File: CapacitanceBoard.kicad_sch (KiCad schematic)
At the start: 1 part, among them U1 AD7150BRMZ

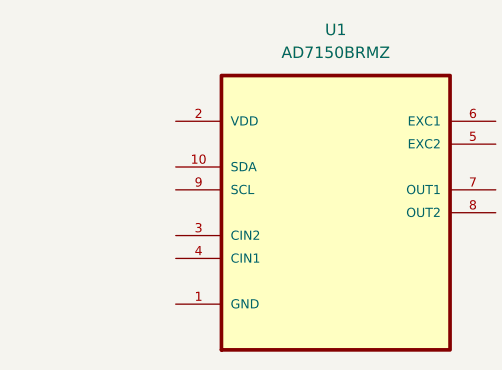
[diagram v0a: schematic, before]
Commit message: Added Mounting Holes
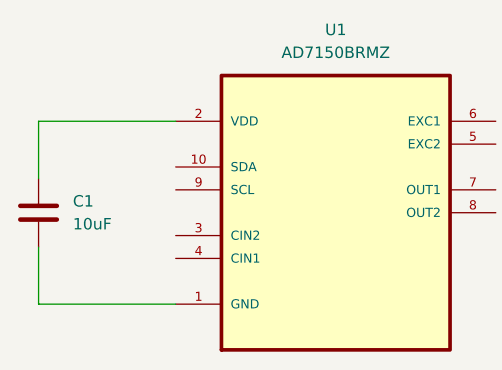
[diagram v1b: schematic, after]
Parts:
- added C1: 10uF, symbol Device:C
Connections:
- net at U1.1 (GND): now also C1.2
- net at U1.2 (VDD): now also C1.1
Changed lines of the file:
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@@
 (kicad_sch (version 20230121) (generator eeschema)
   (paper "A4")
+  (wire (pts (xy 151.13 110.49) (xy 151.13 104.14))
+    (stroke (width 0) (type default))
+  )
+  (wire (pts (xy 151.13 118.11) (xy 151.13 124.46))
+    (stroke (width 0) (type default))
+  )
+  (wire (pts (xy 151.13 104.14) (xy 166.37 104.14))
+    (stroke (width 0) (type default))
+  )
+  (wire (pts (xy 151.13 124.46) (xy 166.37 124.46))
+    (stroke (width 0) (type default))
+  )
+  (symbol (lib_id "Device:C") (at 151.13 114.3 0) (unit 1)
+    (in_bom yes) (on_board yes) (dnp no) (fields_autoplaced)
+    (property "Reference" "C1" (at 154.94 113.03 0)
+      (effects (font (size 1.27 1.27)) (justify left))
+    )
+    (property "Value" "10uF" (at 154.94 115.57 0)
+      (effects (font (size 1.27 1.27)) (justify left))
+    )
+    (property "Footprint" "" (at 152.0952 118.11 0)
+      (effects (font (size 1.27 1.27)) hide)
+    )
+    (property "Datasheet" "~" (at 151.13 114.3 0)
+      (effects (font (size 1.27 1.27)) hide)
+    )
+    (pin "2")
+    (pin "1")
+    (instances
+      (project "CapacitanceBoard"
+        (path "/0af505e0-95df-41c2-86c6-c66100d85f83"
+          (reference "C1") (unit 1)
+        )
+      )
+    )
+  )
   (symbol (lib_id "AD7150BRMZ:AD7150BRMZ") (at 184.15 111.76 0) (unit 1)
     (in_bom yes) (on_board yes) (dnp no) (fields_autoplaced)

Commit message: Added Schematic Files
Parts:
- added C: 47p, symbol Device:C
- added C: 68p, symbol Device:C
- added C2: 10u, symbol Device:C
- added C4: 22p, symbol Device:C
- added R: 39k, symbol Device:R
- added R1, R2: 1k, symbol Device:R
- added R3: 10k, symbol Device:R
- added R4: 82k, symbol Device:R
- C1: value 10uF -> 0.1u
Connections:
- net Earth: now reaches C1.1
- net Earth: now also U1.1 (GND), C.1, C.1, C2.1, C4.1; no longer U1.2 (VDD)
- net VDD: now reaches C1.2
- net VDD: now also U1.2 (VDD), C2.2, R1.2, R2.2; no longer U1.1 (GND)
- net SDA: now reaches U1.10 (SDA)
- net SDA: now also R1.1
- net at U1.4 (CIN1): now also C4.2, R4.1
- net at U1.6 (EXC1): now also C.2, R3.2
- net SCL: now reaches U1.9 (SCL)
- net SCL: now also R2.1
- new net: C.2, R.1, R4.2
- new net Probe: R.2, R3.1

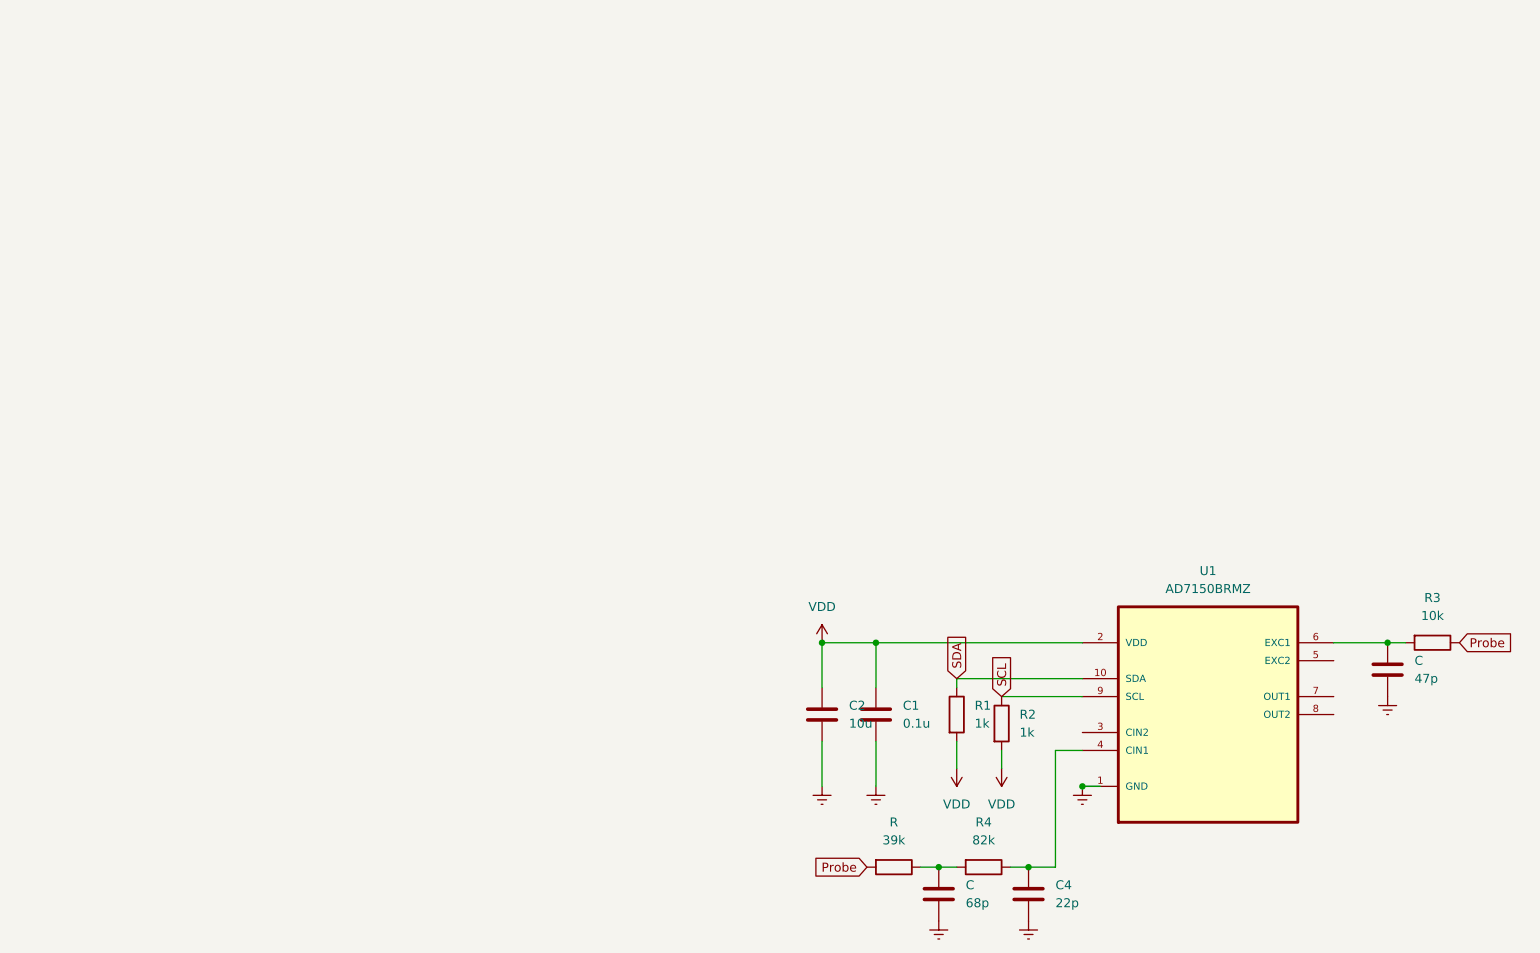
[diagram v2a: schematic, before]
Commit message: Improved schematic and updated PCB references and layout.
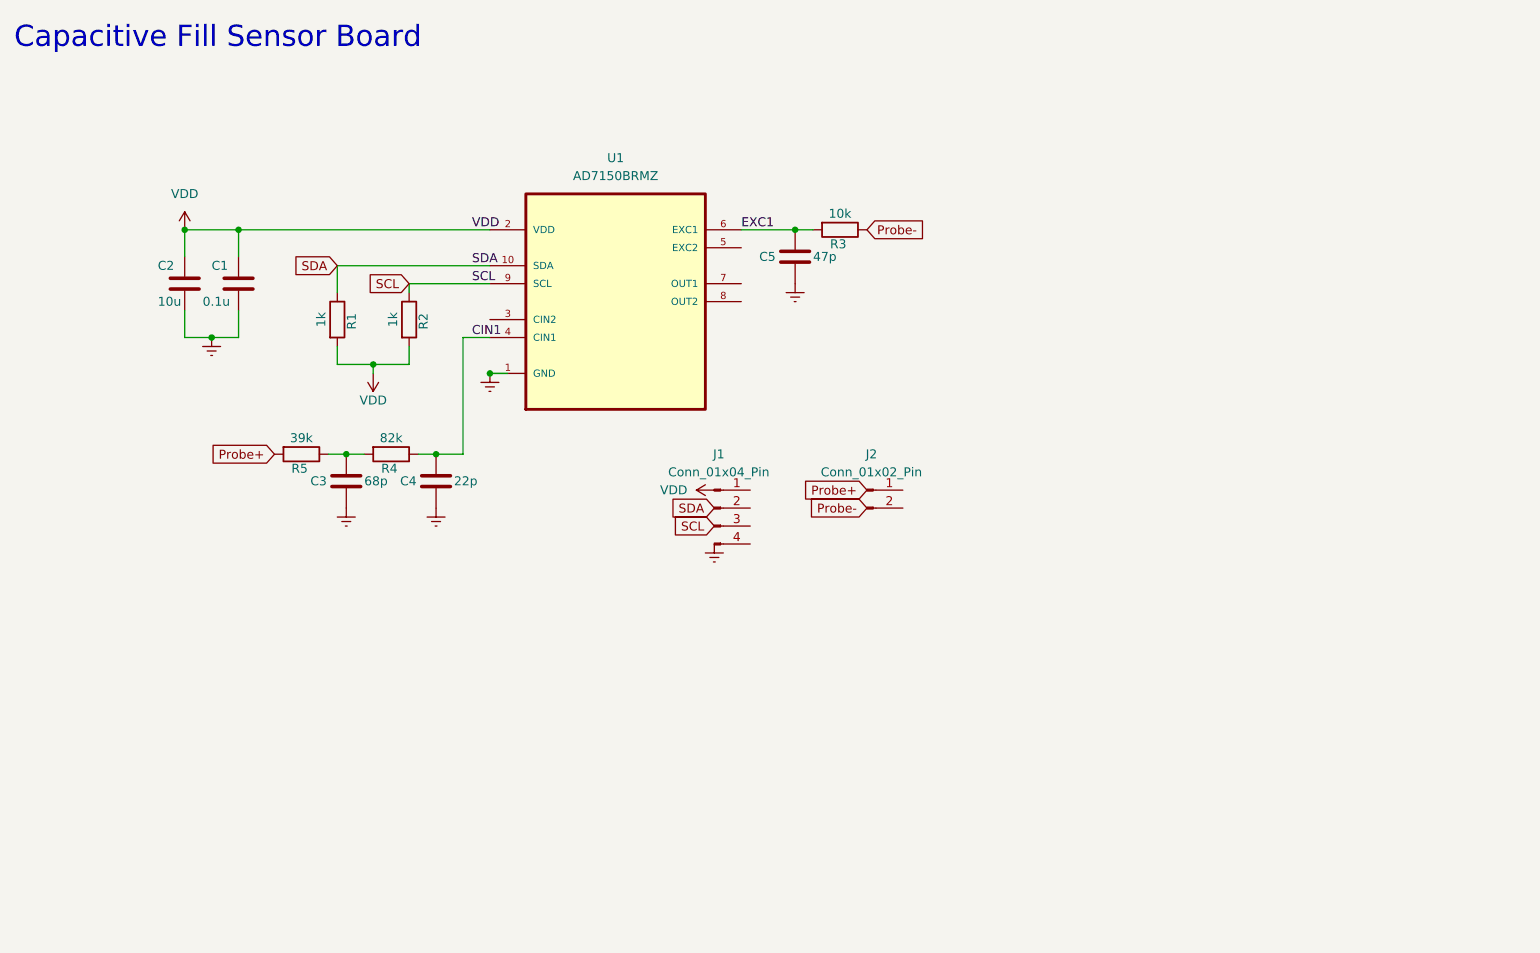
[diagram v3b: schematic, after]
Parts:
- removed C: 47p, symbol Device:C
- removed C: 68p, symbol Device:C
- removed R: 39k, symbol Device:R
- added C3: 68p, Capacitor_SMD:C_0402_1005Metric, symbol Device:C
- added C5: 47p, Capacitor_SMD:C_0402_1005Metric, symbol Device:C
- added J1: Conn_01x04_Pin, Connector_JST:JST_XH_S4B-XH-A_1x04_P2.50mm_Horizontal, symbol Connector:Conn_01x04_Pin
- added J2: Conn_01x02_Pin, Connector_JST:JST_XH_S2B-XH-A_1x02_P2.50mm_Horizontal, symbol Connector:Conn_01x02_Pin
- added R5: 39k, Resistor_SMD:R_0402_1005Metric, symbol Device:R
- C1, C2, C4: footprint (none) -> Capacitor_SMD:C_0402_1005Metric
- R1, R2, R3, R4: footprint (none) -> Resistor_SMD:R_0402_1005Metric
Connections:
- net Earth: now also C1.2, C2.2, C4.2, C3.2, C5.2; no longer C1.1, C2.1, C4.1
- net VDD: now also C1.1, C2.1; no longer C1.2, C2.2
- net EXC1: now reaches R3.2, U1.6 (EXC1)
- net EXC1: now also C5.1
- net CIN1: now reaches R4.1, U1.4 (CIN1)
- net CIN1: now also C4.1; no longer C4.2
- net at R4.2: now also C3.1, R5.1
- net Probe renamed Probe-
- new net Probe+: R5.2
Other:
- note added: "Capacitive Fill Sensor Board"

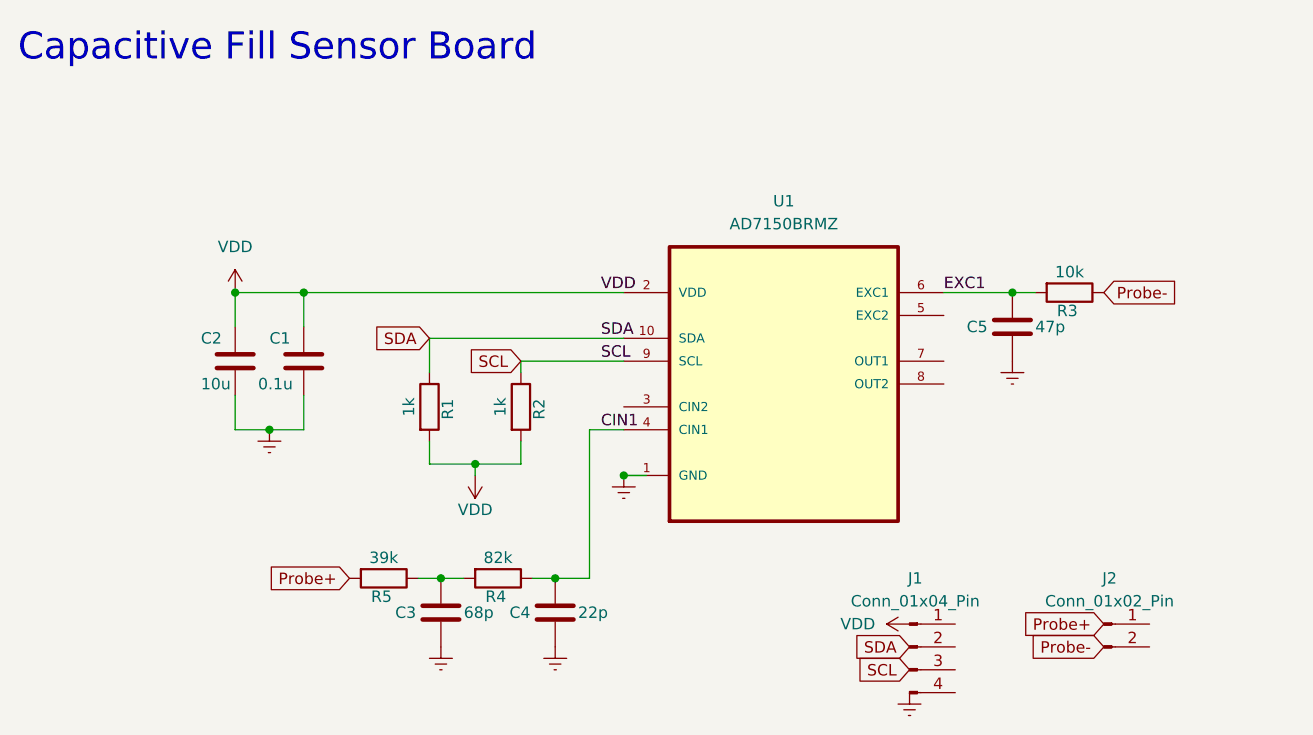
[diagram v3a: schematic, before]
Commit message: Added Second Probe Input
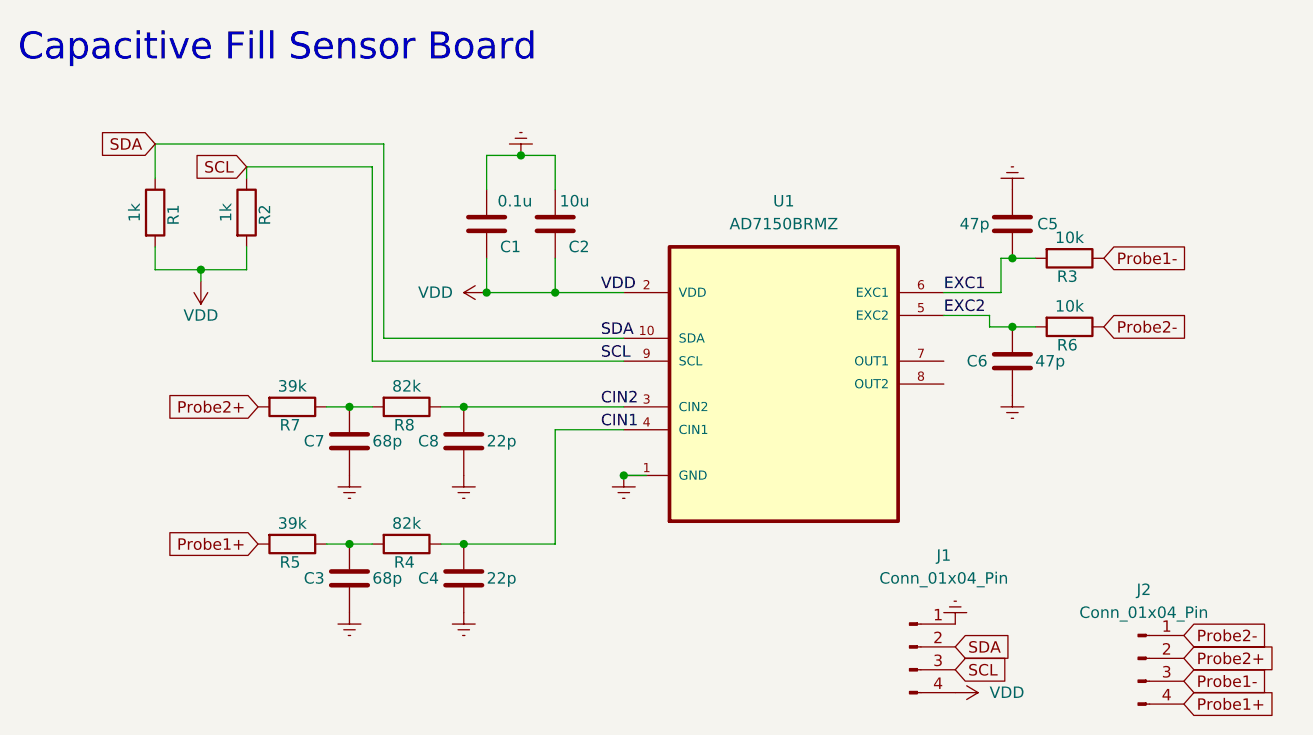
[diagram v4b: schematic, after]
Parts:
- removed J2: Conn_01x02_Pin, Connector_JST:JST_XH_S2B-XH-A_1x02_P2.50mm_Horizontal, symbol Connector:Conn_01x02_Pin
- added C6: 47p, Capacitor_SMD:C_0402_1005Metric, symbol Device:C
- added C7: 68p, Capacitor_SMD:C_0402_1005Metric, symbol Device:C
- added C8: 22p, Capacitor_SMD:C_0402_1005Metric, symbol Device:C
- added J2: Conn_01x04_Pin, Connector_JST:JST_XH_S4B-XH-A_1x04_P2.50mm_Horizontal, symbol Connector:Conn_01x04_Pin
- added R6: 10k, Resistor_SMD:R_0402_1005Metric, symbol Device:R
- added R7: 39k, Resistor_SMD:R_0402_1005Metric, symbol Device:R
- added R8: 82k, Resistor_SMD:R_0402_1005Metric, symbol Device:R
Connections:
- net Earth: now also J1.1 (Pin_1), C6.2, C7.2, C8.2
- net SCL: now also J1.3 (Pin_3)
- net SDA: now also J1.2 (Pin_2)
- net VDD: now also J1.4 (Pin_4)
- net CIN2: now reaches U1.3 (CIN2)
- net CIN2: now also C8.1, R8.1
- net EXC2: now reaches U1.5 (EXC2)
- net EXC2: now also C6.1, R6.2
- net Probe+ renamed Probe1+
- net Probe1+: now also J2.4 (Pin_4)
- net Probe- renamed Probe1-
- net Probe1-: now also J2.3 (Pin_3)
- new net: C7.1, R7.1, R8.2
- new net Probe2+: J2.2 (Pin_2), R7.2
- new net Probe2-: J2.1 (Pin_1), R6.1
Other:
- moved on the sheet: C1, C2, C3, C4, C5, R1, R2, R3, R4, R5
